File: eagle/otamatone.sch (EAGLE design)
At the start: 39 parts, among them IC1 TDA2822M, K1 MK20DX256VLH7, T1 MCP1825S, X1 MINI-USB

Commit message: Incremental updates to schematic and firmware
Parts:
- added SX1: PIN, t32_ref:PIN
- added U$4: VERT_JACK, otamatone:VERT_JACK
- G1: device t32_ref:CRYSTAL-HC49US -> otamatone:CRYSTAL-
- U$3: value MINI-USB -> VERT_USB
- renumbered X1 to U$3
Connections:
- new net VBAT: SX1.P$1, U$1.SW1
- net AGND: now also U$4.GND, U$4.R
- net GND: now also G1.GND
- net N$7: now also U$4.L
- net VIN: now also U$1.SW0

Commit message: Updated schematics
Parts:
- removed C12: 0.1uF, t32_ref:CAPACITOR-0.1UF
- removed P1: (no value), t32_ref:LED
- removed SX10, SX4, SX52, SX9: PIN, t32_ref:PIN
- removed T1: MCP1825S, t32_ref:LDO
- added BTN_GND, S+, SX3, SX5: PINSMT, otamatone:PINSMT
- added BTN_GND1, BTN_GND2: PIN, t32_ref:PIN
- added C15, C3: 10uF, rcl:C-USC0603
- added C16, C17: 0.1uF, rcl:C-USC0603
- added C18: 10nF, rcl:C-USC0603
- added C19: 0.1uF, otamatone:CAPACITOR-0.1UF
- added C20: 2.2uF, otamatone:CAPACITOR-2.2UF
- added LED1: TLLR4400, led:TLLR4400
- added R11: 10K, rcl:R-US_R0603
- added R12, R13: 4.7, rcl:R-US_R0603
- added R14, R15: 10K, rcl:R-US_R0402
- added U$5: LP38691, otamatone:LP38691
- C1: value 0.1uF -> 2.2uF; device t32_ref:CAPACITOR-0.1UF -> otamatone:CAPACITOR-2.2UF
- C10, C11: device t32_ref:CAPACITOR-22PF -> otamatone:CAPACITOR-22PF
- C14: device rcl:C-USC0603 -> rcl:C-USC0402
- C2, C6: device t32_ref:CAPACITOR-2.2UF -> otamatone:CAPACITOR-2.2UF
- C4, C5, C7, C8, C9: device t32_ref:CAPACITOR-0.1UF -> otamatone:CAPACITOR-0.1UF
- IC1: value TDA2822M -> TDA2822MSOP8; device TDA2822M:TDA2822M -> TDA2822M:TDA2822MSOP8
- R1, R10, R9: device t32_ref:RESISTOR-470R -> rcl:R-US_R0402
- R2, R4: device t32_ref:FERRITE -> otamatone:FERRITE
- R3: device t32_ref:RESISTOR-470R -> otamatone:RESISTOR-470R
- R5, R6: device t32_ref:RESISTOR-33R -> otamatone:RESISTOR-33R
- R7: device t32_ref:DIODE_DUAL -> otamatone:DIODE_DUAL
- R8: value 470R -> (none); device t32_ref:RESISTOR-470R -> rcl:R-US_R0603
- S1: value (none) -> MOMENTARY-SWITCH-SPST-SMD-4.5MM; device t32_ref:TACT_SWITCH -> SparkFun-Switches:MOMENTARY-SWITCH-SPST-SMD-4.5MM
- SX2, SX8: value PIN -> PINSMT; device t32_ref:PIN -> otamatone:PINSMT
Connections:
- removed net N$4: C13.1
- removed net N$54: K1.DAC0, SX52.P$1
- new net FULLVOL: K1.DAC0, U$1.POTH
- new net LBUTTON: K1.PTC1, R14.1, SX5.P$1
- new net N$18: C16.1, R12.1
- new net N$21: C17.1, R13.1
- new net N$22: C15.2, C18.1, IC1.INPUT2-
- new net RBUTTON: K1.PTD6, R15.1, SX2.P$1
- new net S+: IC1.OUTPUT1, R12.2, S+.P$1
- new net S-: IC1.OUTPUT2, R13.2, SX3.P$1
- new net SOUND: C13.2, IC1.INPUT1+, R11.2, U$4.L
- new net VOL_OUT: C13.1, U$1.WIPER
- net AGND: now also C16.2, C17.2, C18.2, C3.2, IC1.GND, IC1.INPUT2+, R11.1, U$1.POTL
- net GND: now also BTN_GND.P$1, BTN_GND2.P$1, C19.2, C20.2, R14.2, R15.2, S1.1, U$5.GND, U$5.PAD; no longer C12.2, S1.3, T1.GND, T1.PAD
- net N$31: now also LED1.A; no longer P1.+
- net N$52: now also LED1.C; no longer P1.-
- net N$7: now also C15.1, IC1.INPUT1-; no longer C13.2, U$4.L
- net N$9: now also S1.2; no longer S1.1
- net SCL0: no longer SX9.P$1
- net SDA0: no longer SX10.P$1
- net VCC: now also BTN_GND1.P$1, C19.1, C20.1, C3.1, IC1.VCC, U$5.OUT; no longer C12.1, SV1.1, SX4.P$1, T1.OUT
- net VIN: now also SV1.1, U$5.IN; no longer SX2.P$1, T1.IN
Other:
- note added: "button GND"
- note added: "neck VCC"
- note added: "to do: button pins optional 5v from usb figure out if Vbat diode is necessary"
- moved on the sheet: C1, C4, C5, IC1

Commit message: sync changes
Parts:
- removed R7: (no value), otamatone:DIODE_DUAL
- added U$6, U$7: SCHOTTKY, otamatone:SCHOTTKY
- C9: value 0.1uF -> 2.2uF; device otamatone:CAPACITOR-0.1UF -> otamatone:CAPACITOR-2.2UF
- U$5: value LP38691 -> AP2112K; device otamatone:LP38691 -> otamatone:AP2112K
- renumbered SX3 to S-
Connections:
- removed net N$68: C9.1, K1.VBAT, R7.3
- new net N$1: U$1.SW1, U$6.C, U$7.C
- new net VUSB: C9.1, U$3.1, U$6.A
- net GND: no longer U$5.PAD
- net VBAT: now also U$7.A; no longer U$1.SW1
- net VCC: now also K1.VBAT, U$5.VOUT; no longer R7.1, U$5.OUT
- net VIN: now also U$5.EN, U$5.VIN; no longer U$5.IN
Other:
- note added: "to do: figure out height of button change LDO regulator"
- note removed: "to do: button pins optional 5v from usb figure out if Vbat diode is necessary"
- moved on the sheet: C9

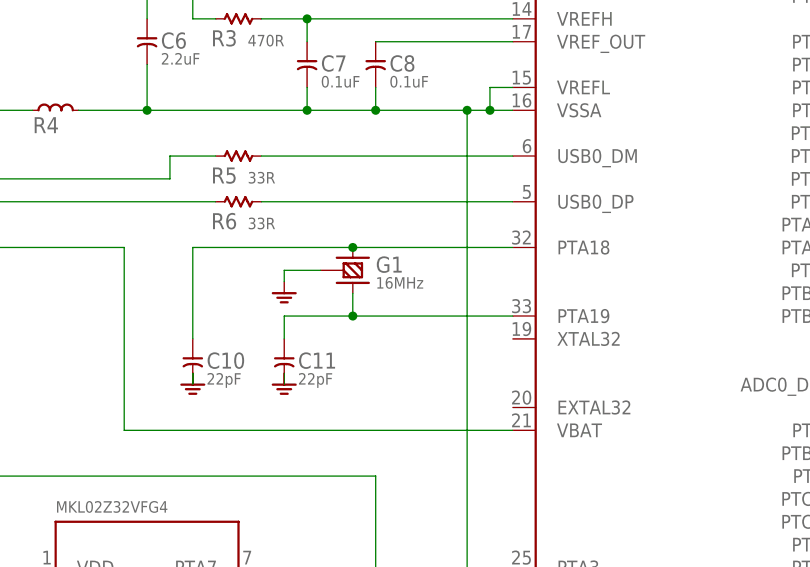
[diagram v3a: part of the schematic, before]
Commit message: Updated gitignore and board contents
unrouted components are now drc compliant, through hole components have been place
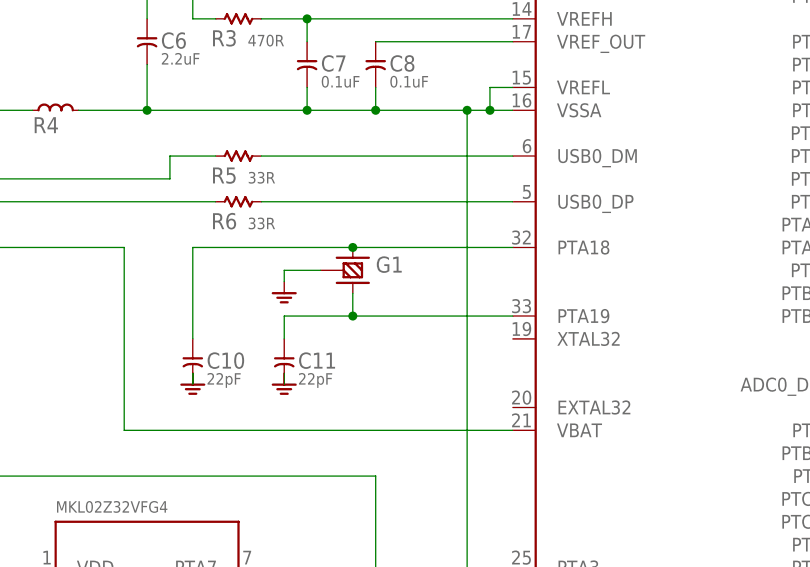
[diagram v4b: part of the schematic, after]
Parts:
- removed BTN_GND1: PIN, t32_ref:PIN
- added Z+: PINSMT, otamatone:PINSMT
- G1: value 16MHz -> (none)
- renumbered BTN_GND2 to B-, SX1 to B+, SX8 to Z-
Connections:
- net VCC: now also Z+.P$1; no longer BTN_GND1.P$1

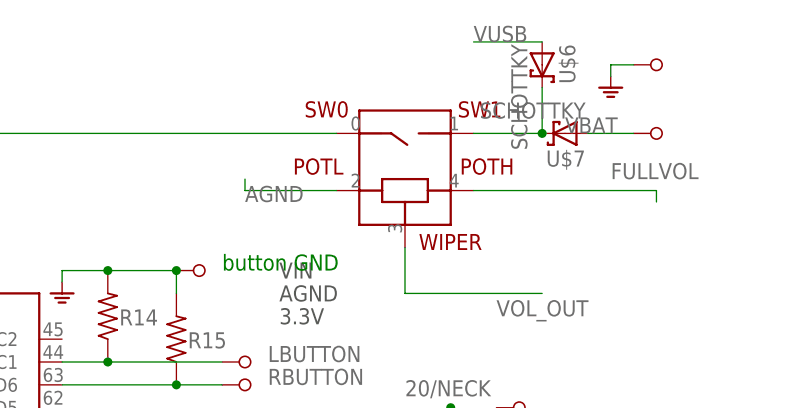
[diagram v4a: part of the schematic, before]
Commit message: started laying out pcb
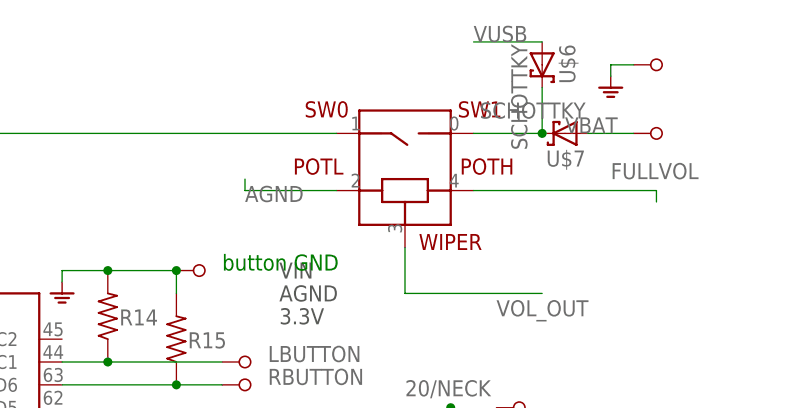
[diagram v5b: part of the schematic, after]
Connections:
- net N$10 renamed USB0_DP
- net N$14 renamed USB0_DM
- net N$16 renamed USB_P
- net N$17 renamed USB_M
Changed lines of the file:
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@@
 <grid distance="0.1" unitdist="inch" unit="inch" style="lines" multiple="1" display="no" altdistance="0.01" altunitdist="inch" altunit="inch"/>
 <layers>
-<layer number="1" name="Top" color="4" fill="1" visible="yes" active="no"/>
-<layer number="2" name="Route2" color="1" fill="3" visible="yes" active="no"/>
-<layer number="3" name="Route3" color="4" fill="3" visible="yes" active="no"/>
-<layer number="4" name="Route4" color="1" fill="4" visible="yes" active="no"/>
-<layer number="5" name="Route5" color="4" fill="4" visible="yes" active="no"/>
-<layer number="6" name="Route6" color="1" fill="8" visible="yes" active="no"/>
-<layer number="7" name="Route7" color="4" fill="8" visible="yes" active="no"/>
-<layer number="8" name="Route8" color="1" fill="2" visible="yes" active="no"/>
-<layer number="9" name="Route9" color="4" fill="2" visible="yes" active="no"/>
-<layer number="10" name="Route10" color="1" fill="7" visible="yes" active="no"/>
-<layer number="11" name="Route11" color="4" fill="7" visible="yes" active="no"/>
-<layer number="12" name="Route12" color="1" fill="5" visible="yes" active="no"/>
-<layer number="13" name="Route13" color="4" fill="5" visible="yes" active="no"/>
-<layer number="14" name="Route14" color="1" fill="6" visible="yes" active="no"/>
-<layer number="15" name="Route15" color="4" fill="6" visible="yes" active="no"/>
-<layer number="16" name="Bottom" color="1" fill="1" visible="yes" active="no"/>
-<layer number="17" name="Pads" color="2" fill="1" visible="yes" active="no"/>
-<layer number="18" name="Vias" color="2" fill="1" visible="yes" active="no"/>
-<layer number="19" name="Unrouted" color="6" fill="1" visible="yes" active="no"/>
-<layer number="20" name="Dimension" color="24" fill="1" visible="yes" active="no"/>
-<layer number="21" name="tPlace" color="7" fill="1" visible="yes" active="no"/>
-<layer number="22" name="bPlace" color="7" fill="1" visible="yes" active="no"/>
-<layer number="23" name="tOrigins" color="15" fill="1" visible="yes" active="no"/>
-<layer number="24" name="bOrigins" color="15" fill="1" visible="yes" active="no"/>
-<layer number="25" name="tNames" color="7" fill="1" visible="yes" active="no"/>
-<layer number="26" name="bNames" color="7" fill="1" visible="yes" active="no"/>
-<layer number="27" name="tValues" color="7" fill="1" visible="yes" active="no"/>
-<layer number="28" name="bValues" color="7" fill="1" visible="yes" active="no"/>
+<layer number="1" name="Top" color="4" fill="1" visible="no" active="no"/>
+<layer number="2" name="Route2" color="1" fill="3" visible="no" active="no"/>
+<layer number="3" name="Route3" color="4" fill="3" visible="no" active="no"/>
+<layer number="4" name="Route4" color="1" fill="4" visible="no" active="no"/>
+<layer number="5" name="Route5" color="4" fill="4" visible="no" active="no"/>
+<layer number="6" name="Route6" color="1" fill="8" visible="no" active="no"/>
+<layer number="7" name="Route7" color="4" fill="8" visible="no" active="no"/>
+<layer number="8" name="Route8" color="1" fill="2" visible="no" active="no"/>
+<layer number="9" name="Route9" color="4" fill="2" visible="no" active="no"/>
+<layer number="10" name="Route10" color="1" fill="7" visible="no" active="no"/>
+<layer number="11" name="Route11" color="4" fill="7" visible="no" active="no"/>
+<layer number="12" name="Route12" color="1" fill="5" visible="no" active="no"/>
+<layer number="13" name="Route13" color="4" fill="5" visible="no" active="no"/>
+<layer number="14" name="Route14" color="1" fill="6" visible="no" active="no"/>
+<layer number="15" name="Route15" color="4" fill="6" visible="no" active="no"/>
+<layer number="16" name="Bottom" color="1" fill="1" visible="no" active="no"/>
+<layer number="17" name="Pads" color="2" fill="1" visible="no" active="no"/>
+<layer number="18" name="Vias" color="2" fill="1" visible="no" active="no"/>
+<layer number="19" name="Unrouted" color="6" fill="1" visible="no" active="no"/>
+<layer number="20" name="Dimension" color="24" fill="1" visible="no" active="no"/>
+<layer number="21" name="tPlace" color="7" fill="1" visible="no" active="no"/>
+<layer number="22" name="bPlace" color="7" fill="1" visible="no" active="no"/>
+<layer number="23" name="tOrigins" color="15" fill="1" visible="no" active="no"/>
+<layer number="24" name="bOrigins" color="15" fill="1" visible="no" active="no"/>
+<layer number="25" name="tNames" color="7" fill="1" visible="no" active="no"/>
+<layer number="26" name="bNames" color="7" fill="1" visible="no" active="no"/>
+<layer number="27" name="tValues" color="7" fill="1" visible="no" active="no"/>
+<layer number="28" name="bValues" color="7" fill="1" visible="no" active="no"/>
 <layer number="29" name="tStop" color="7" fill="3" visible="no" active="no"/>
 <layer number="30" name="bStop" color="7" fill="6" visible="no" active="no"/>
@@
 <layer number="35" name="tGlue" color="7" fill="4" visible="no" active="no"/>
 <layer number="36" name="bGlue" color="7" fill="5" visible="no" active="no"/>
-<layer number="37" name="tTest" color="7" fill="1" visible="yes" active="no"/>
-<layer number="38" name="bTest" color="7" fill="1" visible="yes" active="no"/>
+<layer number="37" name="tTest" color="7" fill="1" visible="no" active="no"/>
+<layer number="38" name="bTest" color="7" fill="1" visible="no" active="no"/>
 <layer number="39" name="tKeepout" color="4" fill="11" visible="no" active="no"/>
 <layer number="40" name="bKeepout" color="1" fill="11" visible="no" active="no"/>
@@
 <layer number="44" name="Drills" color="7" fill="1" visible="no" active="no"/>
 <layer number="45" name="Holes" color="7" fill="1" visible="no" active="no"/>
-<layer number="46" name="Milling" color="3" fill="1" visible="yes" active="no"/>
-<layer number="47" name="Measures" color="7" fill="1" visible="yes" active="no"/>
-<layer number="48" name="Document" color="7" fill="1" visible="yes" active="no"/>
-<layer number="49" name="Reference" color="7" fill="1" visible="yes" active="no"/>
-<layer number="50" name="dxf" color="7" fill="1" visible="yes" active="no"/>
-<layer number="51" name="tDocu" color="7" fill="1" visible="yes" active="no"/>
-<layer number="52" name="bDocu" color="7" fill="1" visible="yes" active="no"/>
-<layer number="53" name="tGND_GNDA" color="7" fill="9" visible="yes" active="no"/>
-<layer number="54" name="bGND_GNDA" color="1" fill="9" visible="yes" active="no"/>
-<layer number="56" name="wert" color="7" fill="1" visible="yes" active="no"/>
-<layer number="57" name="tCAD" color="7" fill="1" visible="yes" active="no"/>
-<layer number="59" name="tCarbon" color="7" fill="1" visible="yes" active="no"/>
-<layer number="60" name="bCarbon" color="7" fill="1" visible="yes" active="no"/>
+<layer number="46" name="Milling" color="3" fill="1" visible="no" active="no"/>
+<layer number="47" name="Measures" color="7" fill="1" visible="no" active="no"/>
+<layer number="48" name="Document" color="7" fill="1" visible="no" active="no"/>
+<layer number="49" name="Reference" color="7" fill="1" visible="no" active="no"/>
+<layer number="50" name="dxf" color="7" fill="1" visible="no" active="no"/>
+<layer number="51" name="tDocu" color="7" fill="1" visible="no" active="no"/>
+<layer number="52" name="bDocu" color="7" fill="1" visible="no" active="no"/>
+<layer number="53" name="tGND_GNDA" color="7" fill="9" visible="no" active="no"/>
+<layer number="54" name="bGND_GNDA" color="1" fill="9" visible="no" active="no"/>
+<layer number="56" name="wert" color="7" fill="1" visible="no" active="no"/>
+<layer number="57" name="tCAD" color="7" fill="1" visible="no" active="no"/>
+<layer number="59" name="tCarbon" color="7" fill="1" visible="no" active="no"/>
+<layer number="60" name="bCarbon" color="7" fill="1" visible="no" active="no"/>
 <layer number="90" name="Modules" color="5" fill="1" visible="no" active="yes"/>
 <layer number="91" name="Nets" color="2" fill="1" visible="yes" active="yes"/>
@@
 </segment>
 </net>
-<net name="N$10" class="0">
+<net name="USB0_DP" class="0">
 <segment>
 <pinref part="K1" gate="G$1" pin="USB0_DP"/>
@@
 </segment>
 </net>
-<net name="N$14" class="0">
+<net name="USB0_DM" class="0">
 <segment>
 <pinref part="K1" gate="G$1" pin="USB0_DM"/>
@@
 </segment>
 </net>
-<net name="N$16" class="0">
+<net name="USB_P" class="0">
 <segment>
 <pinref part="R6" gate="G$1" pin="1"/>
@@
 </segment>
 </net>
-<net name="N$17" class="0">
+<net name="USB_M" class="0">
 <segment>
 <wire x1="17.78" y1="106.68" x2="76.2" y2="106.68" width="0.1524" layer="91"/>
